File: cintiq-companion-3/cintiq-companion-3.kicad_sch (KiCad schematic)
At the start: 8 parts, among them CN1 13HD_fingerpanel, J3 13HD_buttonboard, X1 13HD_eDP, X2 13HD_penpanel

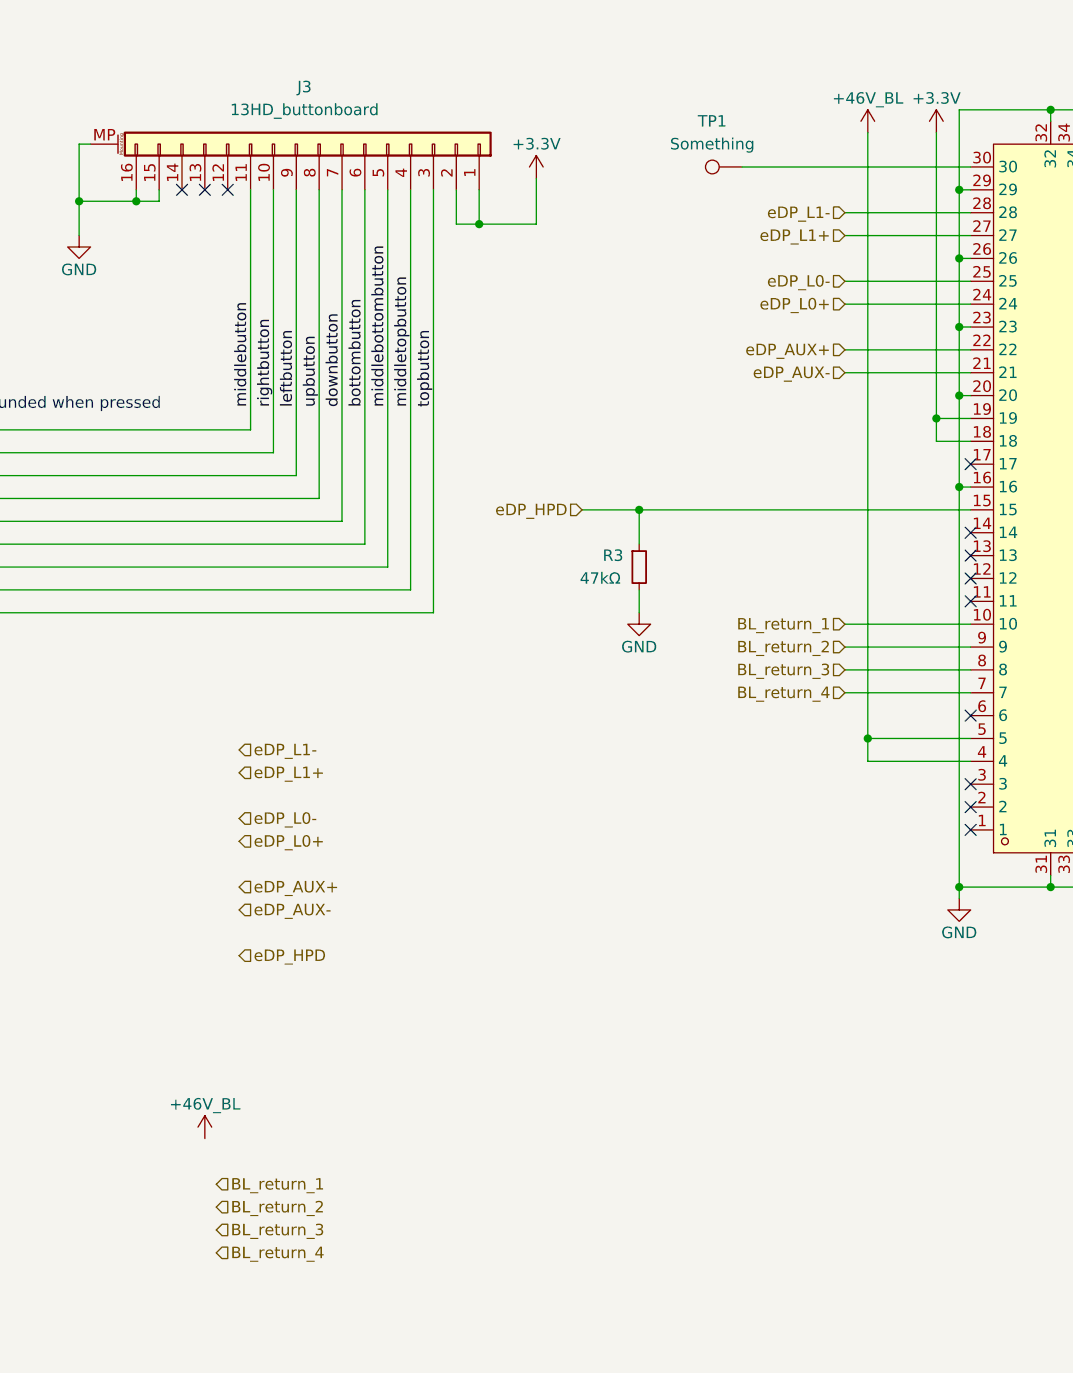
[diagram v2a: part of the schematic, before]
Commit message: Added backlight controller footprint
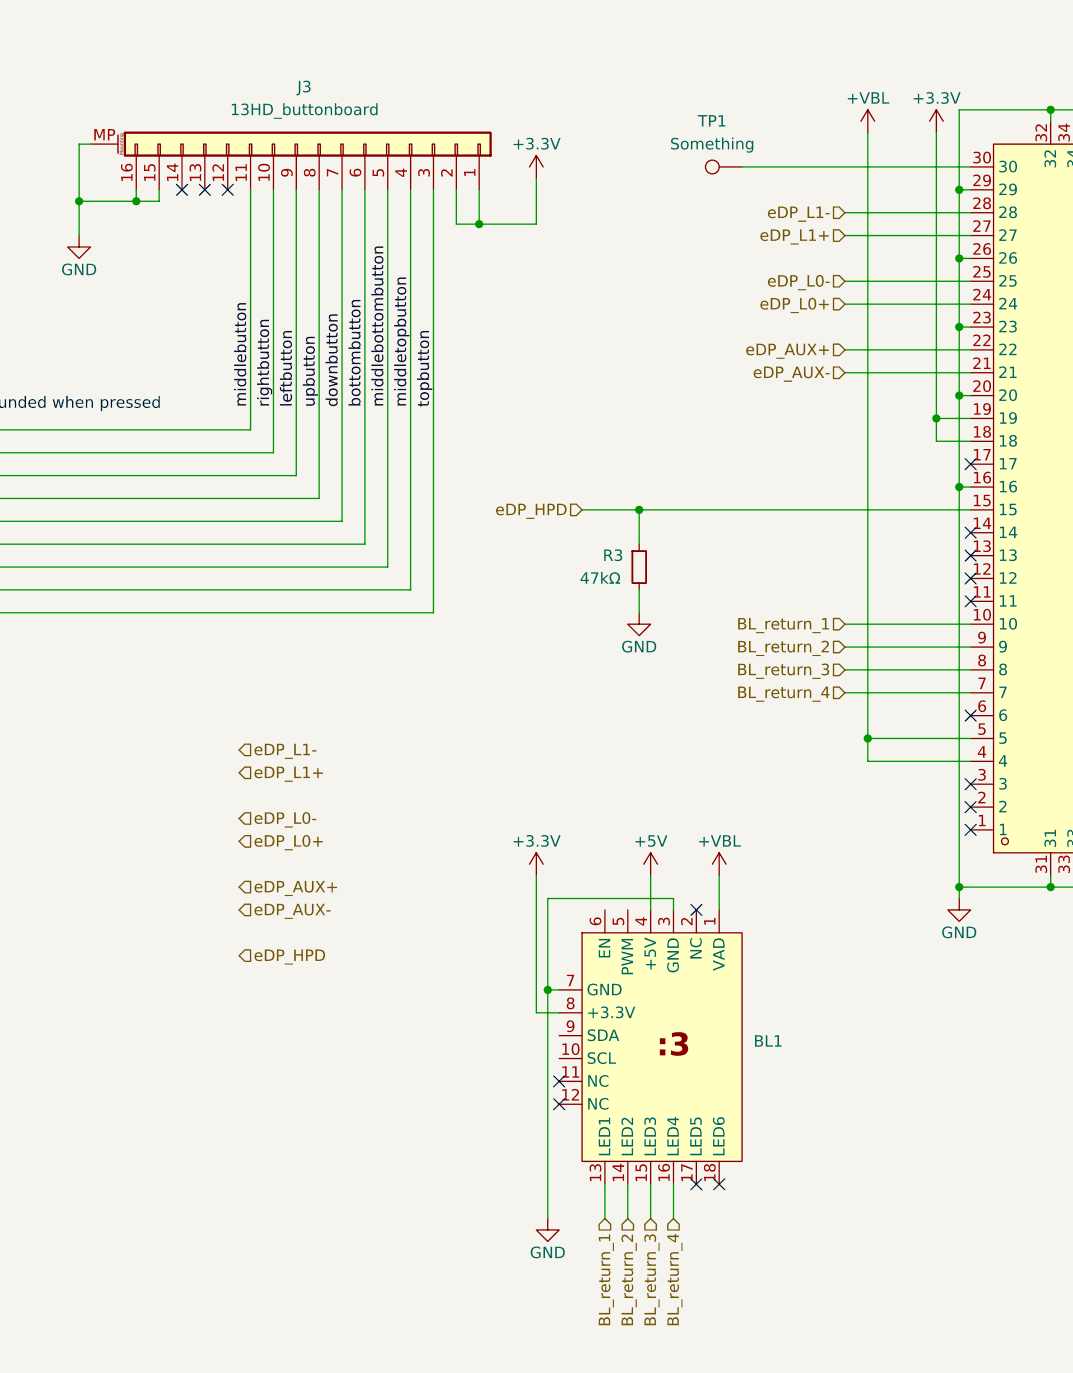
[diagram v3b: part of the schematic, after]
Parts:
- added BL1: ~, A_my_stuff:koyomi-backlight, symbol A_my_stuff:koyomi-backlight
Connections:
- net +3.3V: now also BL1.8 (+3.3V)
- net +5V: now also BL1.4 (+5V)
- net BL_return_1: now also BL1.13 (LED1)
- net BL_return_2: now also BL1.14 (LED2)
- net BL_return_3: now also BL1.15 (LED3)
- net BL_return_4: now also BL1.16 (LED4)
- net GND: now also BL1.3 (GND), BL1.7 (GND)
- net +46V_BL renamed +VBL
- net +VBL: now also BL1.1 (VAD)
- no-connect marks 20 -> 25

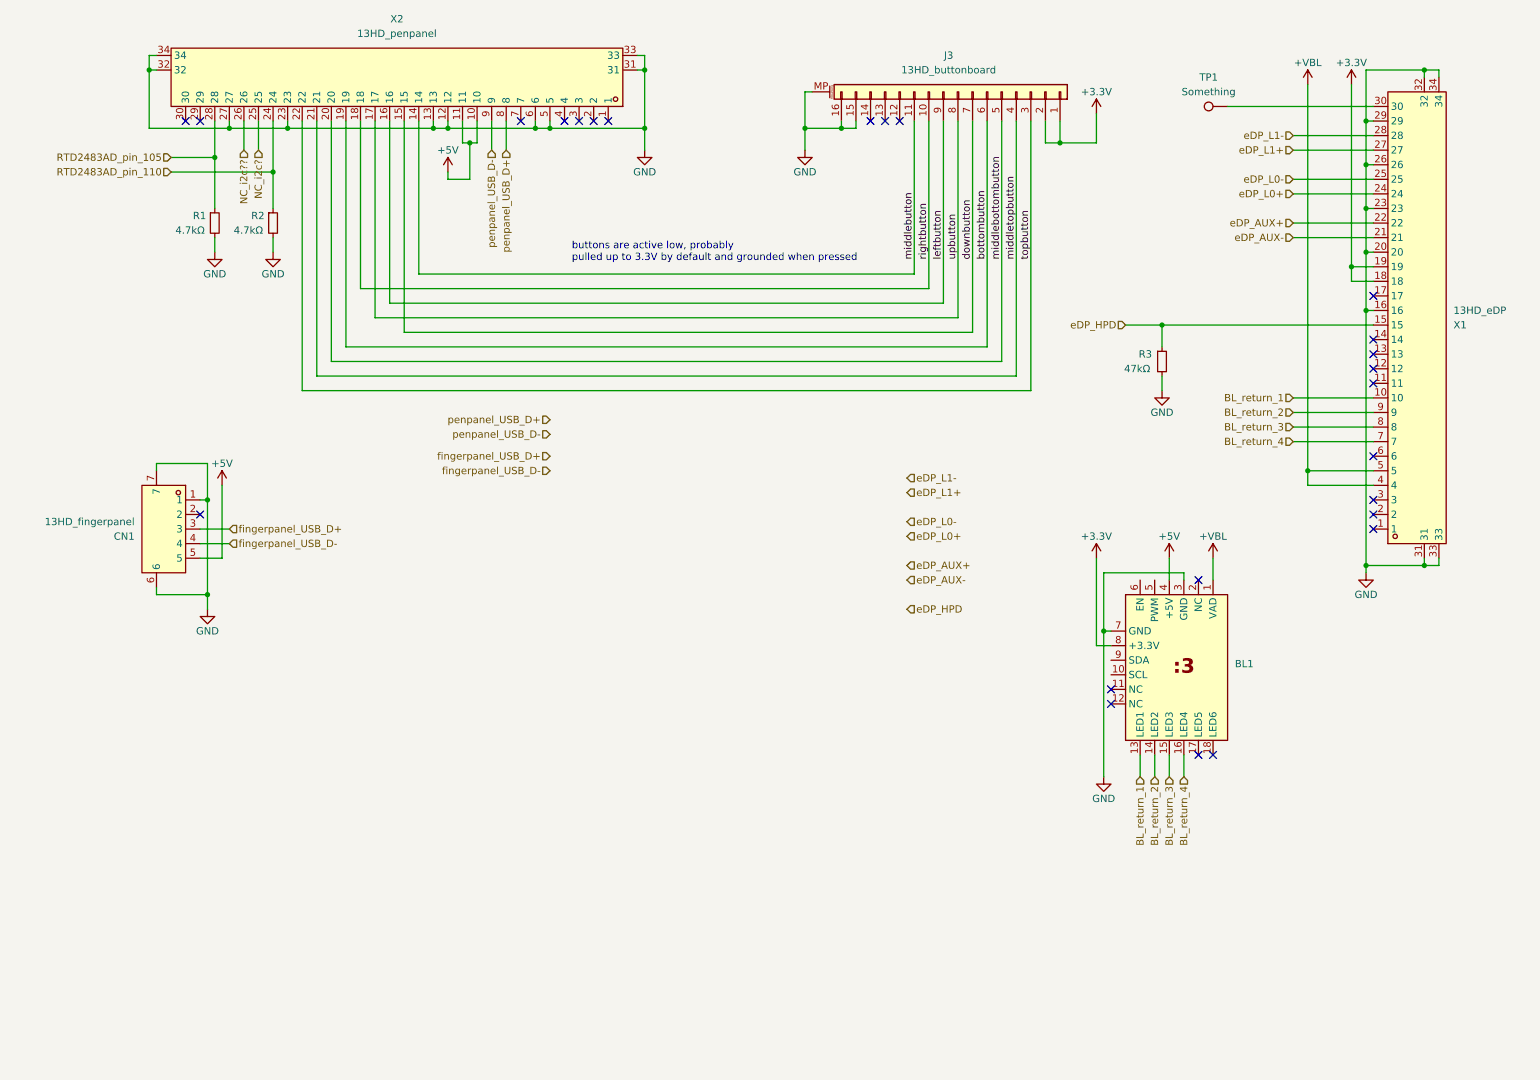
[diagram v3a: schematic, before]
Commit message: Placed mount holes with image measurements but they aren't quite right
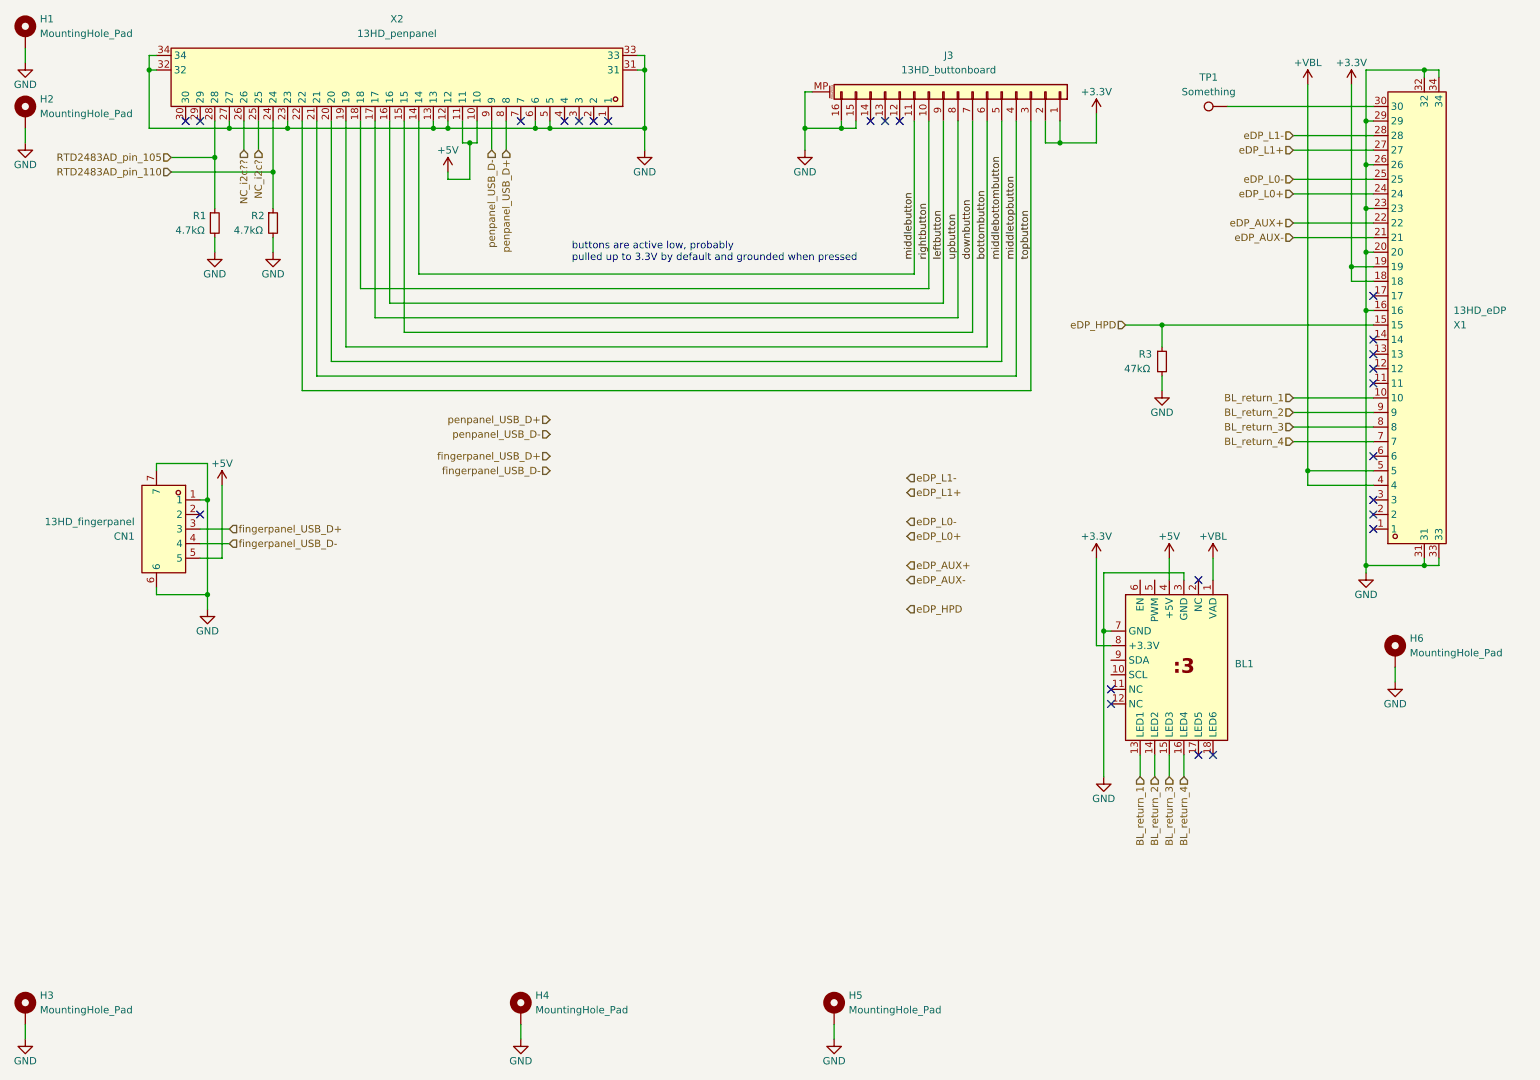
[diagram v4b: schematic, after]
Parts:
- added H1, H2, H3, H4, H5, H6: MountingHole_Pad, MountingHole:MountingHole_2.2mm_M2_DIN965_Pad, symbol Mechanical:MountingHole_Pad
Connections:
- net GND: now also H1.1, H2.1, H3.1, H4.1, H5.1, H6.1

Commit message: schematic and pcb notes lol
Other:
- company: (none) -> WifiCable
- title: (none) -> Cintiq Companion 3
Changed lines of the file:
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@@
 	(generator_version "8.0")
 	(paper "A4")
+	(title_block
+		(title "Cintiq Companion 3")
+		(company "WifiCable")
+	)
 	(junction
 		(at 213.36 67.31)

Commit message: Added LattePanda Mu to schematic
this gonna be cool
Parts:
- removed BL1: ~, A_my_stuff:koyomi-backlight, symbol A_my_stuff:koyomi-backlight
- removed R3: 47kΩ, Resistor_SMD:R_0603_1608Metric, symbol Device:R_Small
- removed TP1: Something, TestPoint:TestPoint_THTPad_D1.5mm_Drill0.7mm, symbol Connector:TestPoint
- removed X1: 13HD_eDP, A_my_stuff:30pipex, symbol A_my_stuff:30pipex
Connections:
- no-connect marks 25 -> 11
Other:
- added sheet 13HD_display (13HD_display.kicad_sch)
- added sheet Mu (Mu.kicad_sch)

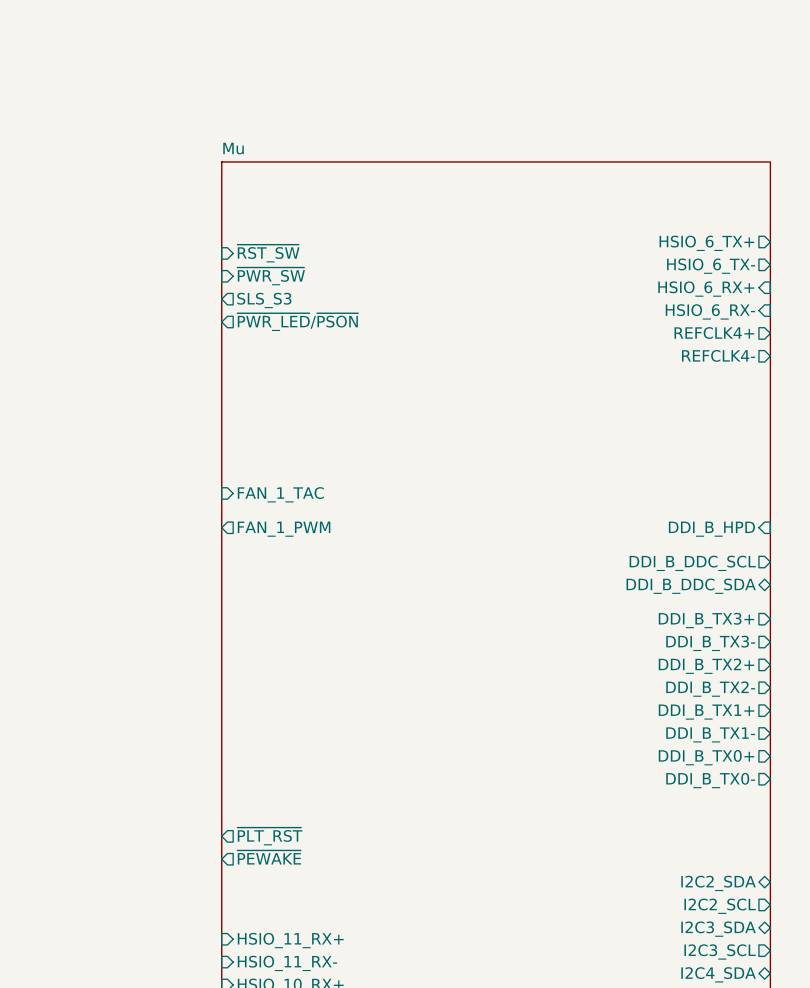
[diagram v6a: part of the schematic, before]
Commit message: Added more Intel diagrams
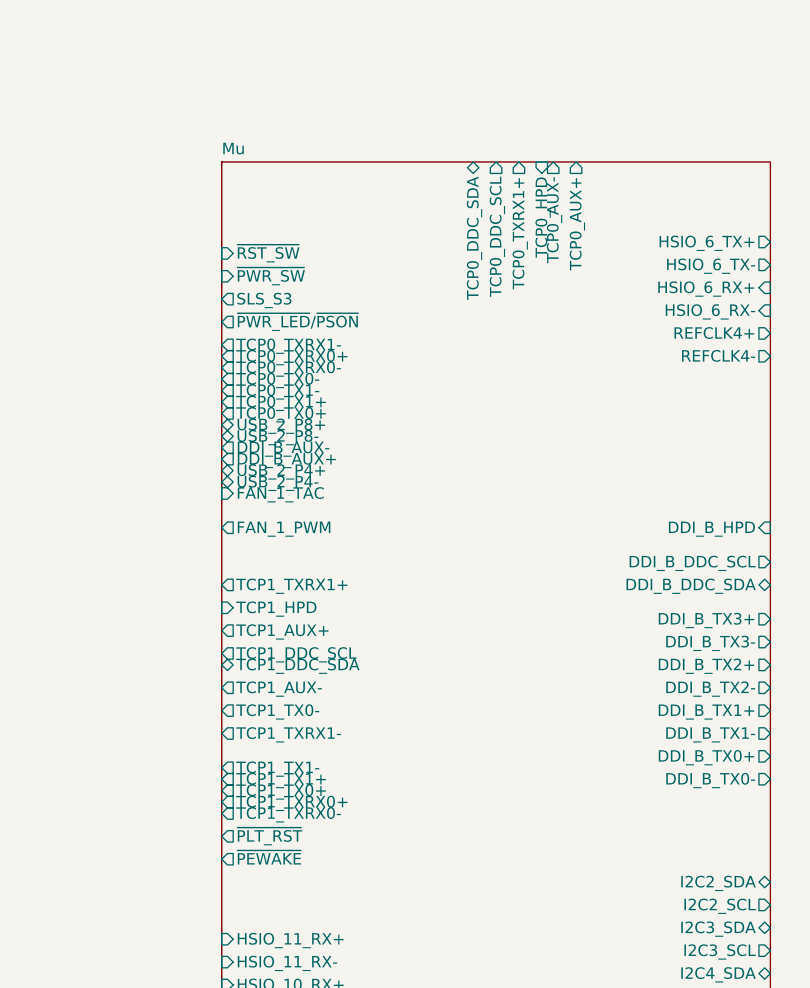
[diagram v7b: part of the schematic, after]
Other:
- sheet Mu ports: added DDI_B_AUX+, DDI_B_AUX-, TCP0_AUX+, TCP0_AUX-, TCP0_DDC_SCL, TCP0_DDC_SDA, TCP0_HPD, TCP0_TX0+, TCP0_TX0-, TCP0_TX1+, TCP0_TX1-, TCP0_TXRX0+, TCP0_TXRX0-, TCP0_TXRX1+, TCP0_TXRX1-, TCP1_AUX+, TCP1_AUX-, TCP1_DDC_SCL, TCP1_DDC_SDA, TCP1_HPD, TCP1_TX0+, TCP1_TX0-, TCP1_TX1+, TCP1_TX1-, TCP1_TXRX0+, TCP1_TXRX0-, TCP1_TXRX1+, TCP1_TXRX1-, USB_2_P4+, USB_2_P4-, USB_2_P8+, USB_2_P8-; removed none

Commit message: Start schematic restructure
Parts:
- removed CN1: 13HD_fingerpanel, A_my_stuff:minitek5p0.8mm, symbol A_my_stuff:minitek5p0.8mm
- removed H1, H2, H3, H4, H5, H6: MountingHole_Pad, MountingHole:MountingHole_2.2mm_M2_DIN965_Pad, symbol Mechanical:MountingHole_Pad
- removed J3: 13HD_buttonboard, Connector_FFC-FPC:Hirose_FH12-16S-0.5SH_1x16-1MP_P0.50mm_Horizontal, symbol Connector_Generic_MountingPin:Conn_01x16_MountingPin
- removed R1, R2: 4.7kΩ, Resistor_SMD:R_0603_1608Metric, symbol Device:R_Small
- removed X2: 13HD_penpanel, A_my_stuff:30pipex, symbol A_my_stuff:30pipex
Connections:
- no-connect marks 11 -> 0
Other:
- removed sheet 13HD_display
- added sheet 13HD_stuff (13HD_stuff.kicad_sch)
- sheet Mu ports: added REFCLK1+, REFCLK1-; removed none
- note added: "Cintiq Companion 3 by WifiCable"
- note removed: "buttons are active low, probably pulled up to 3.3V by default and grounded when pressed"
